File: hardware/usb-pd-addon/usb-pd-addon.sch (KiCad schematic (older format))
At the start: 73 parts, among them J1 Conn_02x10_Odd_Even, J2 Conn_02x10_Odd_Even, J3 USB_TYPE_C, J4 Conn_02x05_Odd_Even, J5 Conn_02x05_Odd_Even, J6 TPAS, J7 TPBS, U1 FUSB302B, U2 AP2171W, U3 SN74AVC1T45DBVR, U4 SN74AVC1T45DBVR, U5 SN74AVC1T45DBVR, U6 SN74AVC1T45DBVR, U7 AP2127K-ADJ, U8 AP2127K-ADJ, U9 NC7SZ125P5X

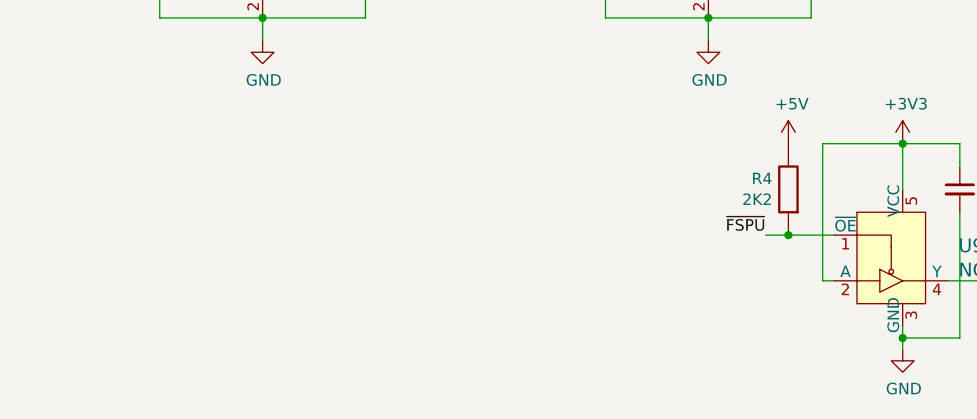
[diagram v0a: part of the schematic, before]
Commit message: Updated README, better silk for voltage control jumpers.
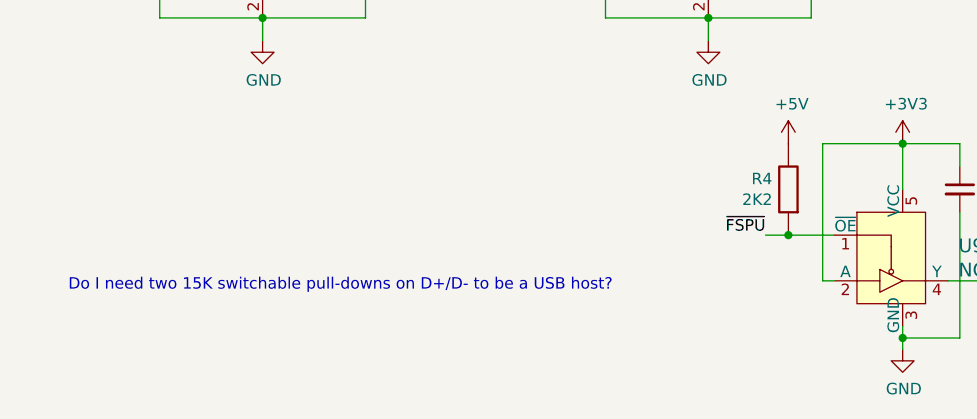
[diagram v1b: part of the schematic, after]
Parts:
- D1, D2: LCSC (none) -> C72043
- U9: LCSC (none) -> C112084
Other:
- note added: "Do I need two 15K switchable pull-downs on D+/D- to be a USB host?"
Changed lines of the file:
@@
 F 11 "ON Semiconductor" H 4750 8200 60  0001 L CNN "Manufacturer"
 F 12 "Active" H 4750 8300 60  0001 L CNN "Status"
+F 13 "C112084" H 4550 7100 50  0001 C CNN "LCSC"
 	1    4550 7100
 	1    0    0    -1
@@
 F 2 "LED_SMD:LED_0603_1608Metric" H 900 2850 50  0001 C CNN
 F 3 "~" H 900 2850 50  0001 C CNN
+F 4 "C72043" V 900 2850 50  0001 C CNN "LCSC"
 	1    900  2850
 	0    -1   -1   0
@@
 F 2 "LED_SMD:LED_0603_1608Metric" H 4250 1850 50  0001 C CNN
 F 3 "~" H 4250 1850 50  0001 C CNN
+F 4 "C72043" V 4250 1850 50  0001 C CNN "LCSC"
 	1    4250 1850
 	0    -1   -1   0
@@
 Wire Wire Line
 	2000 2450 2700 2450
+Text Notes 900  7250 0    50   ~ 0
+Do I need two 15K switchable pull-downs on D+/D- to be a USB host?
 $EndSCHEMATC

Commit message: Remove the D+ pullup, cause Glasgow will not support Luna USB stack.  Added 2 spare SOT23 footprints.
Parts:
- removed C15: 0.1u, pkl_dipol:C_0603, symbol Device:C_Small
- removed R31: 1K5, pkl_dipol:R_0603, symbol pkl_device:pkl_R_Small
- removed U9: NC7SZ125P5X, Package_TO_SOT_SMD:SOT-353_SC-70-5, symbol usb-pd-addon-rescue:NC7SZ125P5X-dk_Logic-Buffers-Drivers-Receivers-Transceivers
- added J8, J9: SPARE, Package_TO_SOT_SMD:SOT-23-6, symbol Connector_Generic:Conn_02x03_Odd_Even
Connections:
- net labels added: A6, A7
- net labels removed: A4, ~FSPU
- wire segments 251 -> 235
- no-connect marks 6 -> 19
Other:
- note removed: "Do I need two 15K switchable pull-downs on D+/D- to be a USB host?"
- moved on the sheet: J3

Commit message: v0.3a: revamped the level shifting, reusing glasgow hardware for 1.8V to 3.3V
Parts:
- removed C6, C8: 1uF, pkl_dipol:C_0603, symbol Device:C_Small
- removed J4, J5: Conn_02x05_Odd_Even, Connector_PinHeader_2.54mm:PinHeader_2x05_P2.54mm_Vertical, symbol Connector_Generic:Conn_02x05_Odd_Even
- removed J8, J9: SPARE, Package_TO_SOT_SMD:SOT-23-6, symbol Connector_Generic:Conn_02x03_Odd_Even
- removed R10: 10k, pkl_dipol:R_0603, symbol pkl_device:pkl_R_Small
- removed R11, R15, R22, R26: 1K2, pkl_dipol:R_0603, symbol pkl_device:pkl_R_Small
- removed R12, R21: 2K0, pkl_dipol:R_0603, symbol pkl_device:pkl_R_Small
- removed R13, R19, R24, R30: 0R, pkl_dipol:R_0603, symbol pkl_device:pkl_R_Small
- removed R14, R23: 4K7, pkl_dipol:R_0603, symbol pkl_device:pkl_R_Small
- removed R16, R25: 6K8, pkl_dipol:R_0603, symbol pkl_device:pkl_R_Small
- removed R17, R28: 1K5, pkl_dipol:R_0603, symbol pkl_device:pkl_R_Small
- removed R18, R27: 10K, pkl_dipol:R_0603, symbol pkl_device:pkl_R_Small
- removed R29: 20K, pkl_dipol:R_0603, symbol pkl_device:pkl_R_Small
- removed U8: AP2127K-ADJ, Package_TO_SOT_SMD:SOT-23-5, symbol Regulator_Linear:AP2127K-ADJ
- added J10, J11, J12, J5: Conn_01x03_Male, Connector_PinHeader_2.54mm:PinHeader_1x03_P2.54mm_Vertical, symbol Connector:Conn_01x03_Male
- added J4: USB_TYPE_C, pkl_connectors:USB_C_Receptacle_HRO_TYPE-C-31-M-12, symbol Connector:USB_C_Receptacle_USB2.0
- added TH4: Mounting_Hole, pkl_pads:ToolingHole, symbol Mechanical:MountingHole
- renumbered R20 to R11, R32 to R13, R7 to R4, R8 to R5, R4 to R6, R5 to R7, R6 to R8
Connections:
- net labels added: 1.2V, SBU1_1V2, SBU2_1V2, USBN_1V2, USBP_1V2
- net labels removed: 1V2_SBU, 1V2_USB, 1V5_SBU, 1V5_USB, 1V8_SBU, 1V8_USB, 2V5_SBU, 2V5_USB, 3V3_SBU, 3V3_USB, ADJ_SBU, VIO_SBU, VIO_USB
- wire segments 235 -> 191
- no-connect marks 19 -> 7
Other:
- moved on the sheet: C5, C7, J3, R11, R9, U7

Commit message: v0.4a: Added decoupling for FUSB302, and protection for DFP mode operation.
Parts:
- removed FID1, FID2: Fiducial, Fiducial:Fiducial_1mm_Mask2mm, symbol Mechanical:Fiducial
- added C6: 1uF, pkl_dipol:C_0603, symbol Device:C_Small
- added C8: 0.1u, pkl_dipol:C_0603, symbol Device:C_Small
- added D3: SMF5.0A, Diode_SMD:D_SOD-123F, symbol Diode:BZD27Cxx
- added J8: Conn_02x03_Odd_Even, Connector_PinHeader_2.54mm:PinHeader_2x03_P2.54mm_Vertical, symbol Connector_Generic:Conn_02x03_Odd_Even
- added JP1, JP2: Jumper_2_Open, Jumper:SolderJumper-2_P1.3mm_Open_RoundedPad1.0x1.5mm, symbol Jumper:Jumper_2_Open
- added TP1, TP2, TP3: TestPoint, TestPoint:TestPoint_THTPad_1.0x1.0mm_Drill0.5mm, symbol Connector:TestPoint
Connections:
- net labels added: AS, VBUS_DFP, VBUS_OUT
- wire segments 191 -> 200
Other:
- moved on the sheet: R5

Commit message: v0.5a: bulk capacitor for 5V supply and lots of protection added, added more silk.
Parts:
- added C16: 150uF, Capacitor_SMD:CP_Elec_6.3x7.7, symbol Device:CP
- added D4, D5: SP3012-06UTG, Glasgow:UDFN-14_3.5x1.35mm_P0.5mm, symbol usb-pd-addon-rescue:SP3012-06UTG-Glasgow
- added D6, D7: SMF20A, Diode_SMD:D_SOD-123F, symbol Diode:BZD27Cxx
- J10, J11, J12, J5: LCSC (none) -> C429954
- J6, J7: LCSC (none) -> C160332
- J8: LCSC (none) -> C65114
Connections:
- net +5V: now also C16.1
- net CC1: now also D4.13 (Ch2), D4.2 (N/C), D5.6 (N/C), D5.9 (Ch5)
- net CC2: now also D4.7 (N/C), D4.8 (Ch6), D5.1 (N/C), D5.14 (Ch1)
- net GND: now also C16.2, D4.10 (GND), D4.5 (N/C), D5.10 (GND), D5.5 (N/C), D6.2 (A), D7.2 (A)
- net SBU1: now also D4.6 (N/C), D4.9 (Ch5), D5.13 (Ch2), D5.2 (N/C)
- net SBU2: now also D4.1 (N/C), D4.14 (Ch1), D5.7 (N/C), D5.8 (Ch6)
- net USBN: now also D4.11 (Ch4), D4.4 (N/C), D5.11 (Ch4), D5.4 (N/C)
- net USBP: now also D4.12 (Ch3), D4.3 (N/C), D5.12 (Ch3), D5.3 (N/C)
- net VBUS: now also J8.3 (Pin_3), D6.1 (K); no longer J8.1 (Pin_1)
- net VBUS_DFP: now also J8.1 (Pin_1); no longer J8.3 (Pin_3)
- net VBUS_OUT: now also D7.1 (K)
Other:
- moved on the sheet: C13, C14, C5, C7, D3, J8, R11, R4, R5, R9, U2, U7

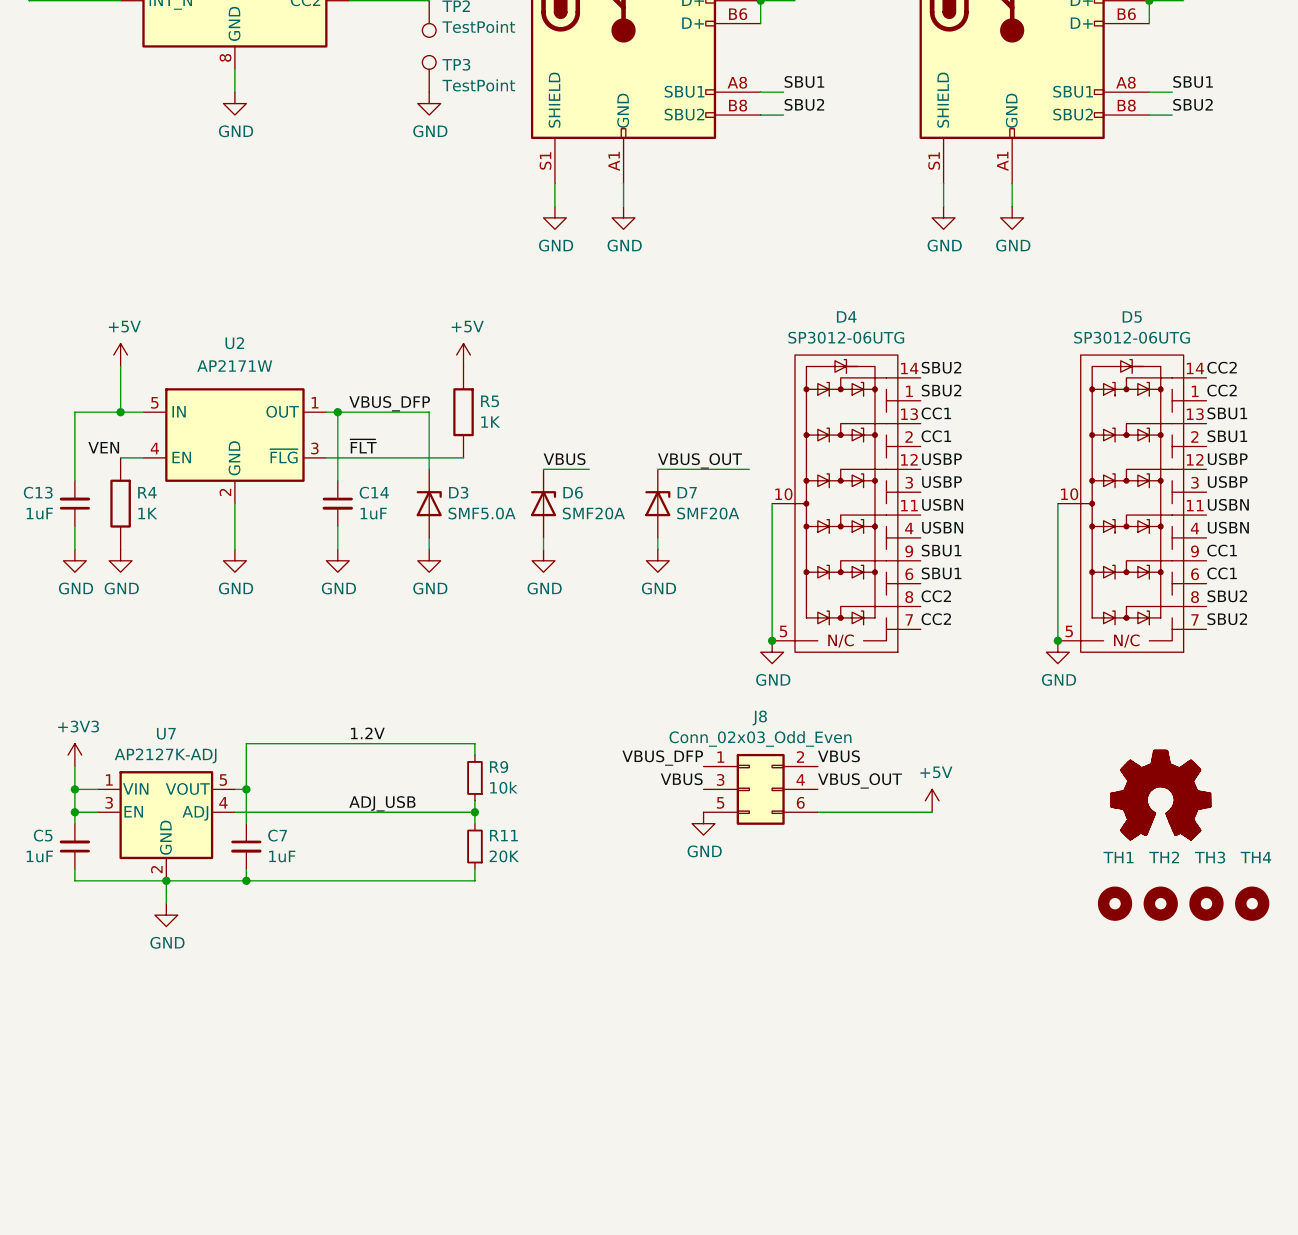
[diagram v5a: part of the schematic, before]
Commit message: v0.6a: Changed to 4 layer board, added caps on CC1/CC2, squared top edge of board, increased silk legibility.
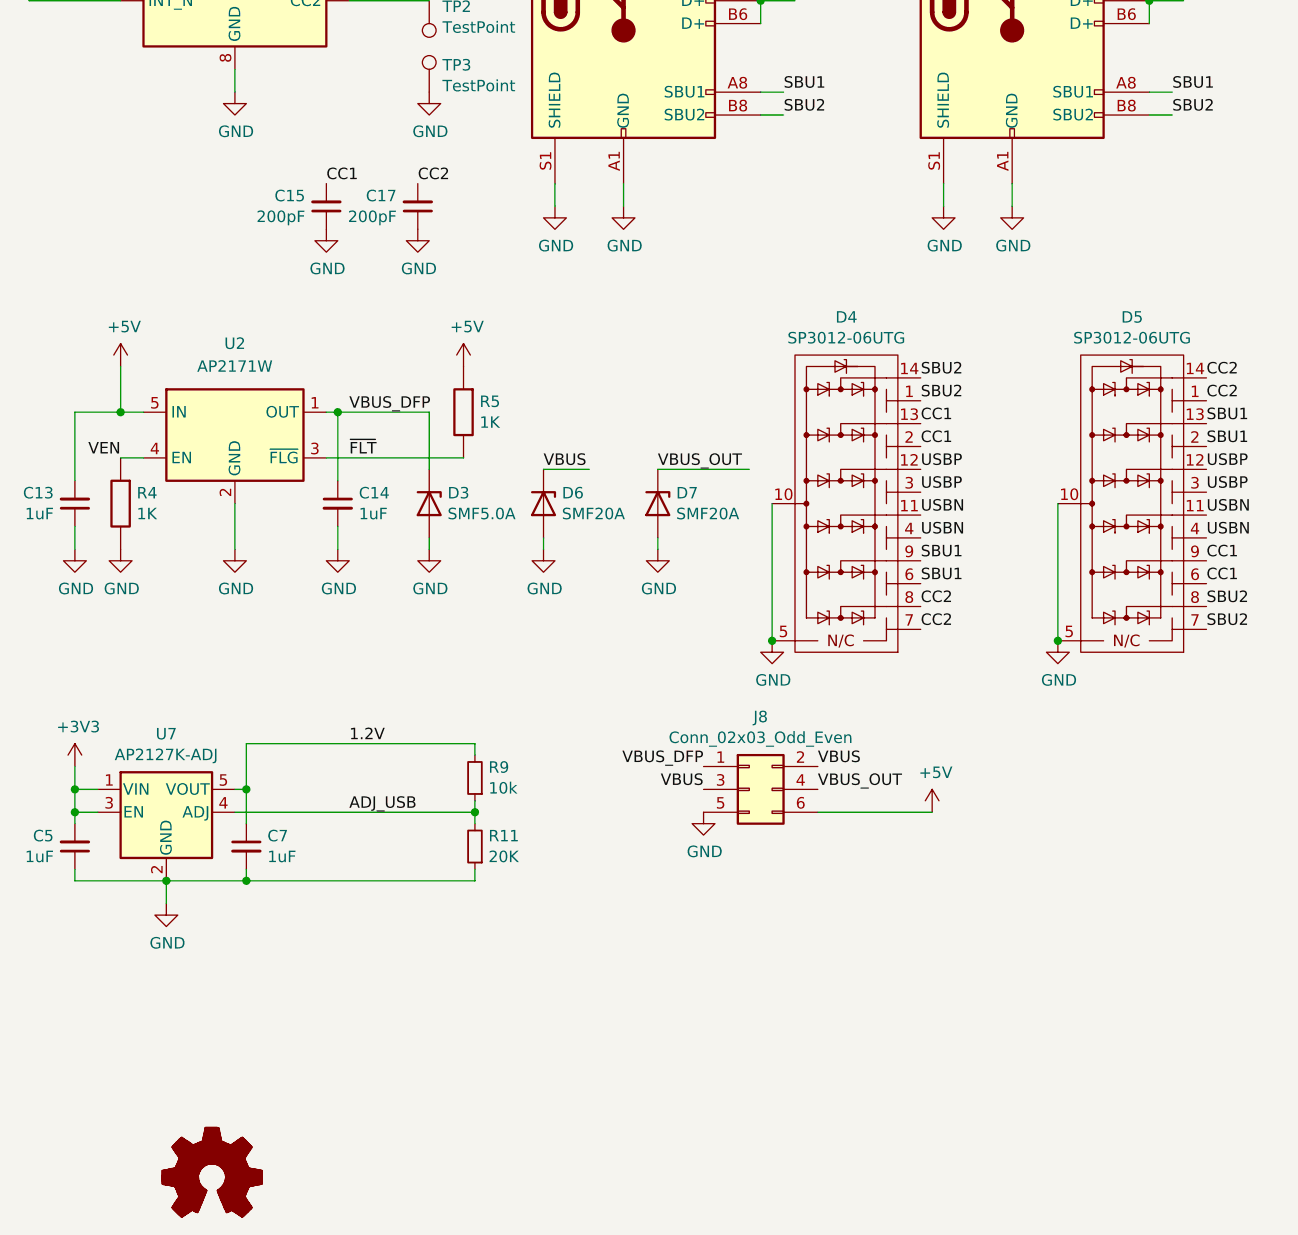
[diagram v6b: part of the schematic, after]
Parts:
- removed TH1, TH2, TH3, TH4: Mounting_Hole, pkl_pads:ToolingHole, symbol Mechanical:MountingHole
- added C15, C17: 200pF, pkl_dipol:C_0603, symbol Device:C_Small
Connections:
- net CC1: now also C15.2
- net CC2: now also C17.2
- net GND: now also C15.1, C17.1
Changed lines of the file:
@@
 NoConn ~ 5200 2250
 NoConn ~ 4900 2250
-$Comp
-L Mechanical:MountingHole MK?
-U 1 1 60844514
-P 10400 6050
-AR Path="/60819140/60844514" Ref="MK?"  Part="1"
-AR Path="/60844514" Ref="TH1"  Part="1"
-F 0 "TH1" H 10350 6250 50  0000 L CNN
-F 1 "Mounting_Hole" H 10500 6010 50  0001 L CNN
-F 2 "pkl_pads:ToolingHole" H 10400 6050 50  0001 C CNN
-F 3 "" H 10400 6050 50  0001 C CNN
-	1    10400 6050
-	1    0    0    -1
-$EndComp
-$Comp
-L Mechanical:MountingHole MK?
-U 1 1 6084451A
-P 10600 6050
-AR Path="/60819140/6084451A" Ref="MK?"  Part="1"
-AR Path="/6084451A" Ref="TH2"  Part="1"
-F 0 "TH2" H 10550 6250 50  0000 L CNN
-F 1 "Mounting_Hole" H 10700 6010 50  0001 L CNN
-F 2 "pkl_pads:ToolingHole" H 10600 6050 50  0001 C CNN
-F 3 "" H 10600 6050 50  0001 C CNN
-	1    10600 6050
-	1    0    0    -1
-$EndComp
-$Comp
-L Mechanical:MountingHole MK?
-U 1 1 60261CA0
-P 10800 6050
-AR Path="/60819140/60261CA0" Ref="MK?"  Part="1"
-AR Path="/60261CA0" Ref="TH3"  Part="1"
-F 0 "TH3" H 10750 6250 50  0000 L CNN
-F 1 "Mounting_Hole" H 10900 6010 50  0001 L CNN
-F 2 "pkl_pads:ToolingHole" H 10800 6050 50  0001 C CNN
-F 3 "" H 10800 6050 50  0001 C CNN
-	1    10800 6050
-	1    0    0    -1
-$EndComp
 Wire Wire Line
 	2950 1550 3450 1550
@@
 L Graphic:Logo_Open_Hardware_Small LOGO1
 U 1 1 6044D04D
-P 10600 5600
-F 0 "LOGO1" H 10600 5875 50  0001 C CNN
-F 1 "Logo_Open_Hardware_Small" H 10600 5375 50  0001 C CNN
-F 2 "Symbol:OSHW-Logo2_7.3x6mm_SilkScreen" H 10600 5600 50  0001 C CNN
-F 3 "~" H 10600 5600 50  0001 C CNN
-	1    10600 5600
+P 6450 7250
+F 0 "LOGO1" H 6450 7525 50  0001 C CNN
+F 1 "Logo_Open_Hardware_Small" H 6450 7025 50  0001 C CNN
+F 2 "Symbol:OSHW-Logo2_7.3x6mm_SilkScreen" H 6450 7250 50  0001 C CNN
+F 3 "~" H 6450 7250 50  0001 C CNN
+	1    6450 7250
 	1    0    0    -1
 $EndComp
@@
 L Graphic:Logo_Open_Hardware_Small LOGO2
 U 1 1 60460712
-P 10600 5600
-F 0 "LOGO2" H 10600 5875 50  0001 C CNN
-F 1 "Logo_Open_Hardware_Small" H 10600 5375 50  0001 C CNN
-F 2 "Symbol:OSHW-Logo2_7.3x6mm_SilkScreen" H 10600 5600 50  0001 C CNN
-F 3 "~" H 10600 5600 50  0001 C CNN
-	1    10600 5600
+P 6450 7250
+F 0 "LOGO2" H 6450 7525 50  0001 C CNN
+F 1 "Logo_Open_Hardware_Small" H 6450 7025 50  0001 C CNN
+F 2 "Symbol:OSHW-Logo2_7.3x6mm_SilkScreen" H 6450 7250 50  0001 C CNN
+F 3 "~" H 6450 7250 50  0001 C CNN
+	1    6450 7250
 	1    0    0    -1
 $EndComp
@@
 $EndComp
 Connection ~ 10550 1400
-$Comp
-L Mechanical:MountingHole TH?
-U 1 1 605480D8
-P 11000 6050
-AR Path="/60819140/605480D8" Ref="TH?"  Part="1"
-AR Path="/605480D8" Ref="TH4"  Part="1"
-F 0 "TH4" H 10950 6250 50  0000 L CNN
-F 1 "Mounting_Hole" H 11100 6010 50  0001 L CNN
-F 2 "pkl_pads:ToolingHole" H 11000 6050 50  0001 C CNN
-F 3 "" H 11000 6050 50  0001 C CNN
-	1    11000 6050
-	1    0    0    -1
-$EndComp
 $Comp
 L Jumper:Jumper_2_Open JP1
@@
 Wire Wire Line
 	8400 4150 8800 4150
+$Comp
+L Device:C_Small C15
+U 1 1 603FA002
+P 6950 3000
+F 0 "C15" H 6858 2954 50  0000 R CNN
+F 1 "200pF" H 6858 3045 50  0000 R CNN
+F 2 "pkl_dipol:C_0603" H 6950 3000 50  0001 C CNN
+F 3 "~" H 6950 3000 50  0001 C CNN
+F 4 "C1600" H 6950 3000 50  0001 C CNN "LCSC"
+	1    6950 3000
+	1    0    0    1
+$EndComp
+$Comp
+L Device:C_Small C17
+U 1 1 603FAA97
+P 7350 3000
+F 0 "C17" H 7258 2954 50  0000 R CNN
+F 1 "200pF" H 7258 3045 50  0000 R CNN
+F 2 "pkl_dipol:C_0603" H 7350 3000 50  0001 C CNN
+F 3 "~" H 7350 3000 50  0001 C CNN
+F 4 "C1600" H 7350 3000 50  0001 C CNN "LCSC"
+	1    7350 3000
+	1    0    0    1
+$EndComp
+Text Label 6950 2900 0    50   ~ 0
+CC1
+Text Label 7350 2900 0    50   ~ 0
+CC2
+$Comp
+L power:GND #PWR035
+U 1 1 603FB2D8
+P 6950 3100
+F 0 "#PWR035" H 6950 2850 50  0001 C CNN
+F 1 "GND" H 6955 2927 50  0000 C CNN
+F 2 "" H 6950 3100 50  0001 C CNN
+F 3 "" H 6950 3100 50  0001 C CNN
+	1    6950 3100
+	1    0    0    -1
+$EndComp
+$Comp
+L power:GND #PWR036
+U 1 1 603FB771
+P 7350 3100
+F 0 "#PWR036" H 7350 2850 50  0001 C CNN
+F 1 "GND" H 7355 2927 50  0000 C CNN
+F 2 "" H 7350 3100 50  0001 C CNN
+F 3 "" H 7350 3100 50  0001 C CNN
+	1    7350 3100
+	1    0    0    -1
+$EndComp
 $EndSCHEMATC
